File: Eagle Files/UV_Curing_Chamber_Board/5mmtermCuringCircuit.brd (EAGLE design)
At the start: 143.2 x 87.5 mm, 29 parts, among them IC1 7805T, IC2 L293D, T1 RFP30N06LE, T2 RFP30N06LE

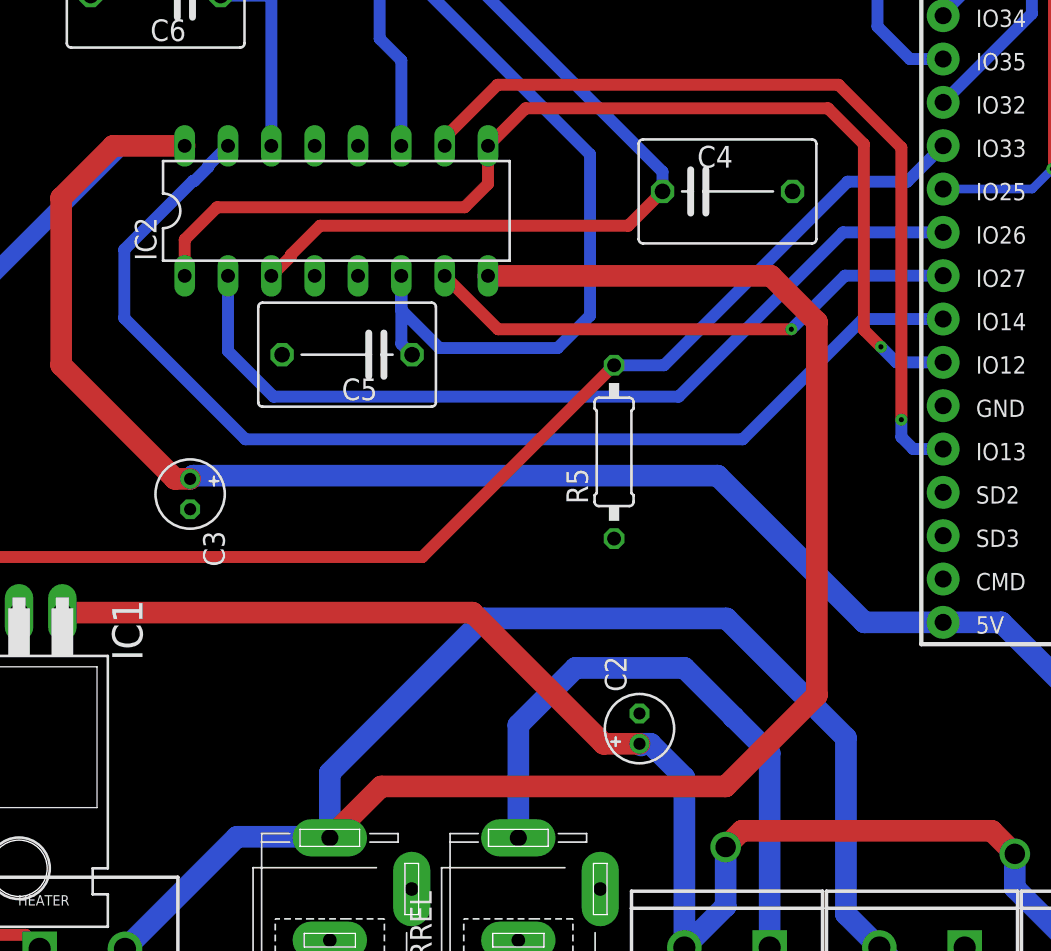
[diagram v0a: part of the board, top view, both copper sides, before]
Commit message: Power changes to motor chip
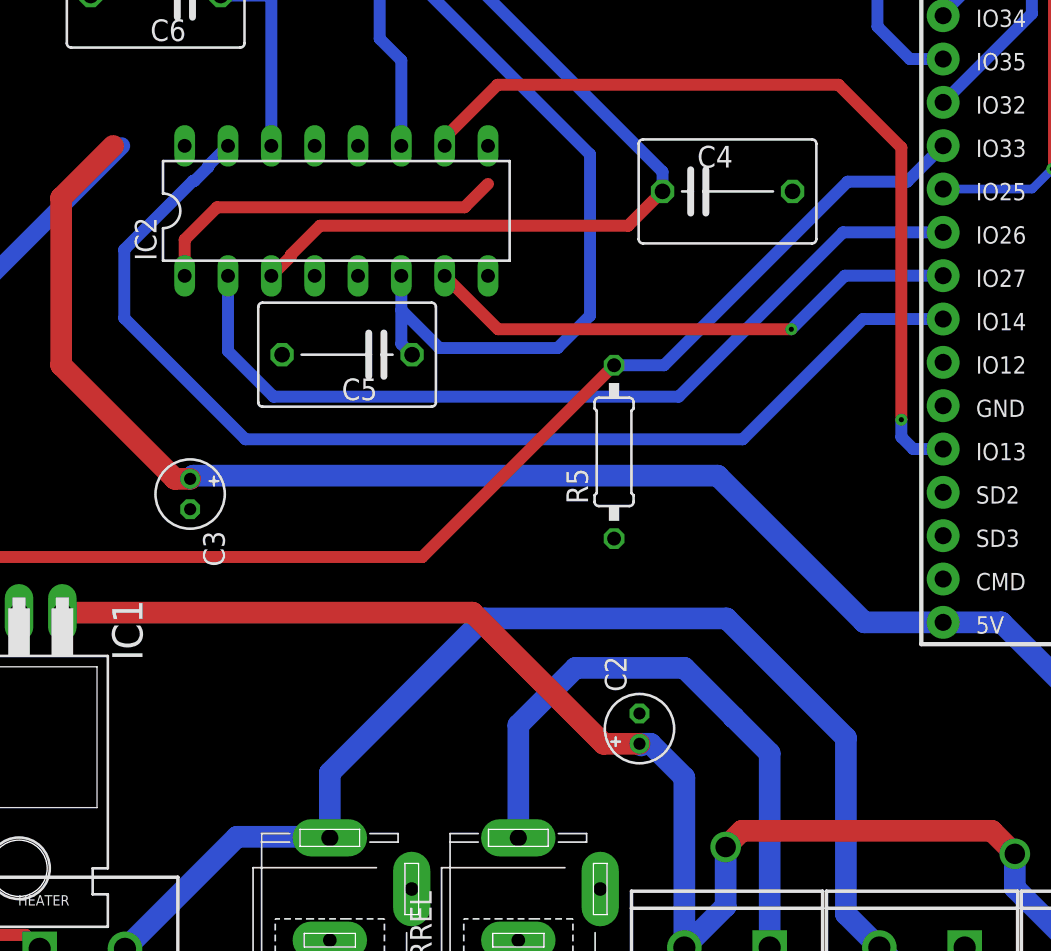
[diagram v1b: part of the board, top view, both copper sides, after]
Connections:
- removed net N$12: IC2.1, IC2.9, U$1.13
- removed net RELAY_NO: FAN.2, HEATER.2, IC2.8, LIGHTS.3, RELAY_B.1
- new net N$28: FAN.2, HEATER.2, LIGHTS.3, RELAY_B.1
- net +5V: now also IC2.1, IC2.8, IC2.9
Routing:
- net RELAY_NO: track 161.2 -> 0.00 mm
- net N$28: track 0.00 -> 86.9 mm
- net N$12: track 63.6 -> 0.00 mm, vias 1 -> 0
- net +5V: track 138.4 -> 151.8 mm
- net N$7: track 46.4 -> 44.4 mm
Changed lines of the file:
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@@
 <?xml version="1.0" encoding="utf-8"?>
 <!DOCTYPE eagle SYSTEM "eagle.dtd">
-<eagle version="9.4.0">
+<eagle version="9.4.1">
 <drawing>
 <settings>
@@
 <vertex x="0.05" y="87.45"/>
 <vertex x="0.05" y="0"/>
-<vertex x="0.05" y="0"/>
 <vertex x="143.1" y="0"/>
 <vertex x="143.1" y="87.45"/>
@@
 <wire x1="130.3458375" y1="35.56" x2="135.5" y2="35.56" width="0.508" layer="16"/>
 </signal>
-<signal name="RELAY_NO" class="1">
-<contactref element="HEATER" pad="2"/>
-<contactref element="FAN" pad="2"/>
-<contactref element="LIGHTS" pad="3"/>
-<contactref element="RELAY_B" pad="1"/>
-<contactref element="IC2" pad="8"/>
-<wire x1="64.46" y1="3.81" x2="62.5" y2="5.77" width="1.27" layer="16"/>
-<wire x1="62.5" y1="5.77" x2="62.5" y2="16.1" width="1.27" layer="16"/>
-<wire x1="62.5" y1="16.1" x2="55.5" y2="23.1" width="1.27" layer="16"/>
-<wire x1="55.5" y1="23.1" x2="41.3" y2="23.1" width="1.27" layer="16"/>
-<wire x1="41.3" y1="23.1" x2="32.249" y2="14.049" width="1.27" layer="16"/>
-<wire x1="32.249" y1="14.049" x2="32.249" y2="10.239" width="1.27" layer="16"/>
-<wire x1="20.24" y1="3.73" x2="26.81" y2="10.3" width="1.27" layer="16"/>
-<wire x1="32.188" y1="10.3" x2="32.249" y2="10.239" width="1.27" layer="16"/>
-<wire x1="26.81" y1="10.3" x2="32.188" y2="10.3" width="1.27" layer="16"/>
-<wire x1="80.89" y1="3.81" x2="78.58" y2="1.5" width="1.27" layer="16"/>
-<wire x1="66.77" y1="1.5" x2="64.46" y2="3.81" width="1.27" layer="16"/>
-<wire x1="78.58" y1="1.5" x2="66.77" y2="1.5" width="1.27" layer="16"/>
-<wire x1="58.10634375" y1="43.18" x2="60.8" y2="40.48634375" width="1.27" layer="1"/>
-<wire x1="60.8" y1="18.6" x2="55.45" y2="13.25" width="1.27" layer="1"/>
-<wire x1="35.26" y1="13.25" x2="32.249" y2="10.239" width="1.27" layer="1"/>
-<wire x1="41.52" y1="43.18" x2="58.10634375" y2="43.18" width="1.27" layer="1"/>
-<wire x1="60.8" y1="40.48634375" x2="60.8" y2="18.6" width="1.27" layer="1"/>
-<wire x1="55.45" y1="13.25" x2="35.26" y2="13.25" width="1.27" layer="1"/>
-</signal>
 <signal name="N$6">
 <contactref element="SPEAKER" pad="2"/>
@@
 <wire x1="26.28" y1="38.77" x2="28.95" y2="36.1" width="0.7" layer="16"/>
 <wire x1="52.7" y1="36.1" x2="62.33" y2="45.73" width="0.7" layer="16"/>
-</signal>
-<signal name="N$12">
-<contactref element="IC2" pad="1"/>
-<contactref element="IC2" pad="9"/>
-<contactref element="U$1" pad="13"/>
-<wire x1="23.74" y1="43.18" x2="23.74" y2="45.3" width="0.7" layer="1"/>
-<wire x1="23.74" y1="45.3" x2="25.64" y2="47.2" width="0.7" layer="1"/>
-<wire x1="41.52" y1="48.57" x2="41.52" y2="50.8" width="0.7" layer="1"/>
-<wire x1="25.64" y1="47.2" x2="40.15" y2="47.2" width="0.7" layer="1"/>
-<wire x1="40.15" y1="47.2" x2="41.52" y2="48.57" width="0.7" layer="1"/>
-<wire x1="65.4598375" y1="38.11" x2="64.55" y2="39.0198375" width="0.7" layer="16"/>
-<via x="64.55" y="39.0198375" extent="1-16" drill="0.3"/>
-<wire x1="63.55" y1="50.9" x2="63.55" y2="40.0198375" width="0.7" layer="1"/>
-<wire x1="64.55" y1="39.0198375" x2="63.55" y2="40.0198375" width="0.7" layer="1"/>
-<wire x1="63.55" y1="50.9" x2="61.45" y2="53" width="0.7" layer="1"/>
-<wire x1="43.72" y1="53" x2="41.52" y2="50.8" width="0.7" layer="1"/>
-<wire x1="68.2" y1="38.11" x2="65.4598375" y2="38.11" width="0.7" layer="16"/>
-<wire x1="61.45" y1="53" x2="43.72" y2="53" width="0.7" layer="1"/>
 </signal>
 <signal name="N$2">
@@
 <contactref element="C3" pad="+"/>
 <contactref element="IC1" pad="3"/>
-<contactref element="IC2" pad="16"/>
 <contactref element="R1" pad="2"/>
 <contactref element="U$1" pad="19"/>
 <contactref element="C1" pad="1"/>
-<wire x1="23.74" y1="50.8" x2="20.04" y2="50.8" width="1.016" layer="16"/>
 <wire x1="20.04" y1="50.8" x2="11.49" y2="42.25" width="1.016" layer="16"/>
 <wire x1="11.49" y1="42.25" x2="11.49" y2="23.44" width="1.016" layer="16"/>
@@
 <wire x1="16.5" y1="37.95" x2="16.5" y2="47.75" width="1.27" layer="1"/>
 <wire x1="16.5" y1="47.75" x2="19.55" y2="50.8" width="1.27" layer="1"/>
-<wire x1="19.55" y1="50.8" x2="23.74" y2="50.8" width="1.27" layer="1"/>
 <wire x1="24.06" y1="31.279" x2="24.25" y2="31.469" width="1.27" layer="16"/>
 <wire x1="63.58" y1="22.87" x2="68.2" y2="22.87" width="1.27" layer="16"/>
@@
 <wire x1="81.54" y1="8.79" x2="78.11" y2="12.22" width="1.27" layer="16"/>
 <wire x1="81.54" y1="8.79" x2="87.36" y2="8.79" width="1.27" layer="16"/>
+<contactref element="IC2" pad="8"/>
+<contactref element="IC2" pad="1"/>
+<wire x1="23.74" y1="43.18" x2="23.74" y2="45.3" width="0.7" layer="1"/>
+<wire x1="23.74" y1="45.3" x2="25.64" y2="47.2" width="0.7" layer="1"/>
+<wire x1="25.64" y1="47.2" x2="40.15" y2="47.2" width="0.7" layer="1"/>
+<wire x1="40.15" y1="47.2" x2="41.52" y2="48.57" width="0.7" layer="1"/>
+<contactref element="IC2" pad="16"/>
+<contactref element="IC2" pad="9"/>
+<wire x1="41.52" y1="48.57" x2="41.52" y2="50.8" width="0" layer="19" extent="1-1"/>
+<wire x1="23.74" y1="50.8" x2="25.64" y2="47.2" width="0" layer="19" extent="1-1"/>
+<wire x1="20.04" y1="50.8" x2="23.74" y2="50.8" width="0" layer="19" extent="16-16"/>
+<wire x1="19.55" y1="50.8" x2="20.04" y2="50.8" width="0" layer="19" extent="1-16"/>
+<wire x1="41.52" y1="43.18" x2="40.15" y2="47.2" width="0" layer="19" extent="1-1"/>
 </signal>
 <signal name="+3V3">
@@
 </signal>
 <signal name="N$7">
-<contactref element="IC2" pad="6"/>
 <contactref element="MOTOR_BREAKOUT" pad="2"/>
-<contactref element="C5" pad="1"/>
 <wire x1="37.71" y1="63.5" x2="37.71" y2="60.09" width="0.7" layer="16"/>
 <wire x1="47.5" y1="50.3" x2="37.71" y2="60.09" width="0.7" layer="16"/>
 <wire x1="45.6" y1="38.95" x2="38.67" y2="38.95" width="0.7" layer="16"/>
 <wire x1="38.67" y1="38.95" x2="36.44" y2="41.18" width="0.7" layer="16"/>
-<wire x1="36.44" y1="43.18" x2="36.44" y2="41.18" width="0.7" layer="16"/>
 <wire x1="45.6" y1="38.95" x2="47.5" y2="40.85" width="0.7" layer="16"/>
 <wire x1="47.5" y1="40.85" x2="47.5" y2="50.3" width="0.7" layer="16"/>
+<contactref element="IC2" pad="6"/>
+<contactref element="C5" pad="1"/>
 <wire x1="37.07" y1="38.56" x2="36.44" y2="39.19" width="0.7" layer="16"/>
 <wire x1="36.44" y1="39.19" x2="36.44" y2="43.18" width="0.7" layer="16"/>
+<wire x1="37.07" y1="38.56" x2="38.67" y2="38.95" width="0" layer="19" extent="16-16"/>
 </signal>
 <signal name="N$15">
@@
 <wire x1="72.4" y1="7.3" x2="75.89" y2="3.81" width="1.27" layer="16"/>
 </signal>
+<signal name="N$28" class="1">
+<contactref element="HEATER" pad="2"/>
+<contactref element="FAN" pad="2"/>
+<contactref element="LIGHTS" pad="3"/>
+<contactref element="RELAY_B" pad="1"/>
+<wire x1="64.46" y1="3.81" x2="62.5" y2="5.77" width="1.27" layer="16"/>
+<wire x1="62.5" y1="5.77" x2="62.5" y2="16.1" width="1.27" layer="16"/>
+<wire x1="62.5" y1="16.1" x2="55.5" y2="23.1" width="1.27" layer="16"/>
+<wire x1="55.5" y1="23.1" x2="41.3" y2="23.1" width="1.27" layer="16"/>
+<wire x1="41.3" y1="23.1" x2="32.249" y2="14.049" width="1.27" layer="16"/>
+<wire x1="32.249" y1="14.049" x2="32.249" y2="10.239" width="1.27" layer="16"/>
+<wire x1="20.24" y1="3.73" x2="26.81" y2="10.3" width="1.27" layer="16"/>
+<wire x1="32.188" y1="10.3" x2="32.249" y2="10.239" width="1.27" layer="16"/>
+<wire x1="26.81" y1="10.3" x2="32.188" y2="10.3" width="1.27" layer="16"/>
+<wire x1="80.89" y1="3.81" x2="78.58" y2="1.5" width="1.27" layer="16"/>
+<wire x1="66.77" y1="1.5" x2="64.46" y2="3.81" width="1.27" layer="16"/>
+<wire x1="78.58" y1="1.5" x2="66.77" y2="1.5" width="1.27" layer="16"/>
+</signal>
 </signals>
